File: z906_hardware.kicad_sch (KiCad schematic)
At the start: 23 parts, among them J1 USB_C_Receptacle_USB2.0_14P, J3 DE_15 Amplifier, J4 DE15 Console, U1 ESP32-S3-WROOM-1, U2 AP63203WU, U3 PCM5102A, U4 TPD2EUSB30, U5 TPD1E05U06DYA, U6 TPS7A4533, U7 PCM1860DBT

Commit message: esp32 power
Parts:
- added C10: 10uF, symbol Device:C
- added C11: 1uF, symbol Device:C
- added C9: 0.1uF, symbol Device:C
- added R4: 0, symbol Device:R
- added R5: 10K, symbol Device:R
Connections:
- net +3.3V: now also C10.1, C9.1, R4.1
- net GND: now also C10.2, C11.2, C9.2
- net +3.3V_esp: now reaches U1.2 (3V3)
- net +3.3V_esp: now also R4.2, R5.1
- net at U1.3 (EN): now also C11.1, R5.2
- net GPIO19 renamed USB_DN
- net GPIO20 renamed USB_DP
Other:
- moved on the sheet: U1

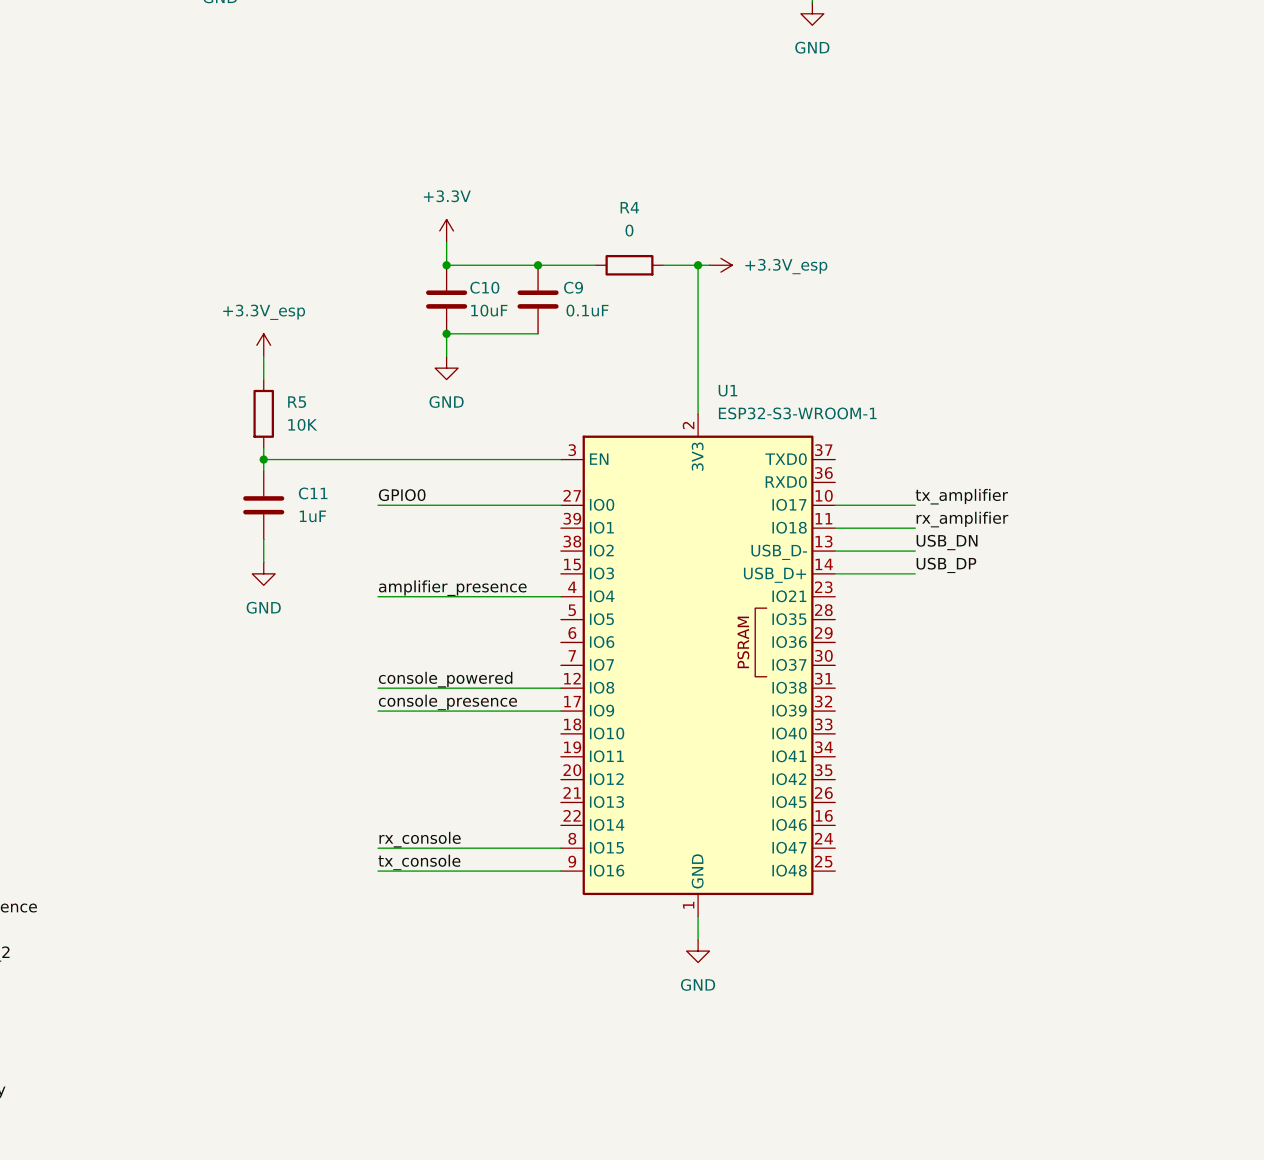
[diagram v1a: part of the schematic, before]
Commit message: jumper boot and reset
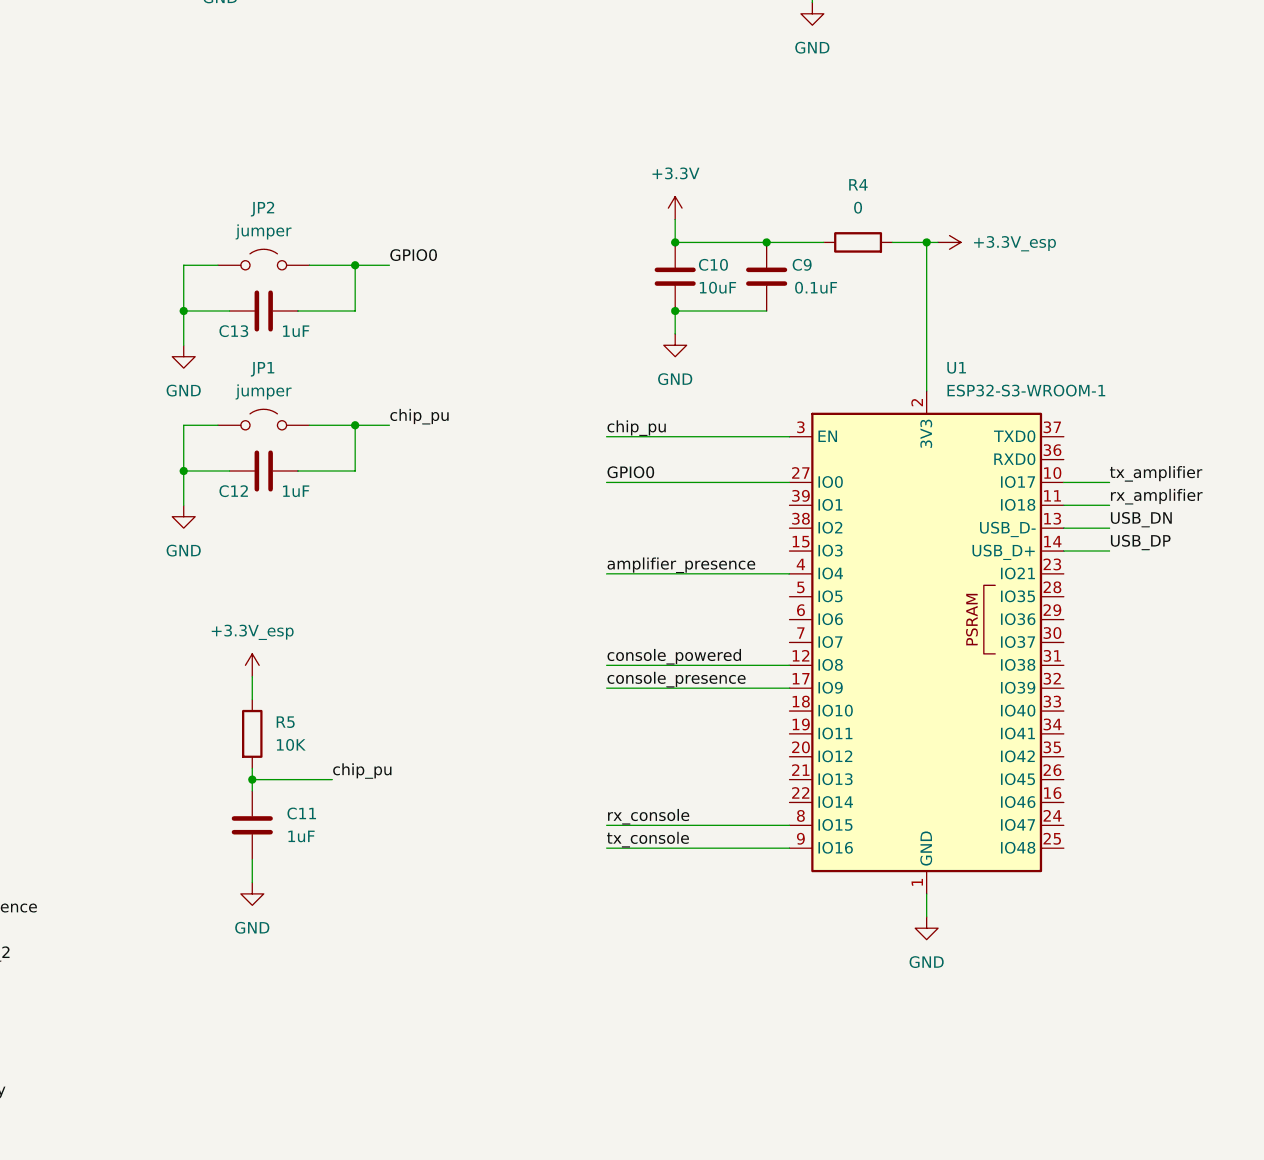
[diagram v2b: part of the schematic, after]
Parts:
- added C12, C13: 1uF, symbol Device:C
- added JP1, JP2: jumper, TestPoint:TestPoint_2Pads_Pitch2.54mm_Drill0.8mm, symbol Jumper:Jumper_2_Open
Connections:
- net GND: now also C12.1, C13.1, JP1.1 (A), JP2.1 (A)
- net GPIO0: now also C13.2, JP2.2 (B)
- net chip_pu: now reaches C11.1, R5.2, U1.3 (EN)
- net chip_pu: now also C12.2, JP1.2 (B)
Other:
- moved on the sheet: C10, C11, C9, R4, R5, U1

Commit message: PCM5102A
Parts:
- added C14, C16, C18, C21: 10uF, symbol Device:C
- added C15, C17, C19, C20: 0.1uF, symbol Device:C
- added C22, C23: 2.2uF, symbol Device:C
- added C24, C25: 2200pF, symbol Device:C
- added R6, R7: 470, symbol Device:R
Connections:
- net +3.3V: now also U3.17 (XSMT), U3.20 (DVDD), C16.1, C17.1
- net +3.3VA: now also U3.1 (CPVDD), U3.8 (AVDD), C14.1, C15.1, C18.1, C19.1
- net GND: now also U3.10 (DEMP), U3.11 (FLT), U3.12 (SCK), U3.16 (FMT), U3.19 (DGND), U3.3 (CPGND), U3.9 (AGND), C14.2, C15.2, C16.2, C17.2, C18.2, C19.2, C20.2, C21.2, C23.2, C24.2, C25.2
- net aux_left: now also C24.1, R6.2
- net aux_right: now also C25.1, R7.2
- net LCK: now reaches U1.5 (IO5)
- net LCK: now also U3.15 (LRCK)
- net BCK: now reaches U1.6 (IO6)
- net BCK: now also U3.13 (BCK)
- net DIN: now reaches U1.7 (IO7)
- net DIN: now also U3.14 (DIN)
- net at U3.18 (LDOO): now also C20.1, C21.1
- net at U3.2 (CAPP): now also C22.1
- net at U3.4 (CAPM): now also C22.2
- net at U3.5 (VNEG): now also C23.1
- net at U3.6 (OUTL): now also R6.1
- net at U3.7 (OUTR): now also R7.1
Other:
- moved on the sheet: C10, C11, C12, C13, C2, C3, C4, C5, C6, C7, C8, C9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

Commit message: PCM1860DBT
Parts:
- added C26, C28, C30, C32: 10uF, symbol Device:C
- added C27, C29, C31, C33: 0.1uF, symbol Device:C
- added C34: 1uF, symbol Device:C
- added C35, C37: 4.7uF, symbol Device:C
- added C36, C38: 1nF, symbol Device:C
- added J2: AudioJack3, symbol Connector_Audio:AudioJack3
- added R10, R11: 100k, symbol Device:R
- added R12, R9: 100, symbol Device:R
- added R8: 10K, symbol Device:R
- added U8: TPD2E2U06DCK, Package_TO_SOT_SMD:SOT-323_SC-70, symbol Power_Protection:TPD2E2U06DCK
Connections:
- net +3.3V: now also U7.13 (DVDD), U7.14 (IOVDD), C26.1, C27.1, C28.1, C29.1, R8.1
- net +3.3VA: now also U7.8 (AVDD), C30.1, C31.1
- net BCK: now also U7.17 (BCK)
- net GND: now also U7.10 (XI), U7.12 (DGND), U7.20 (MD6), U7.21 (MD5), U7.22 (MD4), U7.23 (MD2), U7.24 (MD3), U7.25 (MD1), U7.26 (MD0), U7.7 (AGND), C26.2, C27.2, C28.2, C29.2, C30.2, C31.2, C32.2, C33.2, C34.2, C36.1, C38.1, J2.S, R10.1, R11.1, U8.3; no longer U3.12 (SCK)
- net LCK: now also U7.16 (LRCK)
- net at U7.11 (LDO): now also C32.1, C33.1
- net MCLK: now reaches U7.15 (SCKI)
- net MCLK: now also U1.19 (IO11), U3.12 (SCK)
- net ADC_DATA: now reaches U7.18 (DOUT)
- net ADC_DATA: now also U1.7 (IO7)
- net at U7.19 (INT): now also R8.2
- net at U7.3 (VINL1/VIN1P): now also C36.2, R9.2
- net at U7.4 (VINR1/VIN2P): now also C38.2, R12.2
- net at U7.6 (VREF): now also C34.1
- net DAC_DATA: now reaches U1.18 (IO10)
- net DAC_DATA: now also U3.14 (DIN)
- removed net DIN: U1.7 (IO7), U3.14 (DIN)
- new net: C35.1, J2.T, R10.2, U8.1
- new net: C37.1, J2.R, R11.2, U8.2
- new net: C37.2, R12.1
- new net: C35.2, R9.1
- no-connect marks 2 -> 9
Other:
- moved on the sheet: C10, C11, C12, C13, C14, C15, C16, C17, C18, C19, C20, C21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

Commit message: various correction
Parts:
- removed FB1: 600 Ohm @ 100 Mhz, 500ma, symbol Device:FerriteBead
- removed R3: 4.7, symbol Device:R
- removed R8: 10K, symbol Device:R
- C10: value 10uF -> 22uF
- C12, C13: value 1uF -> 0.1uF
- C24, C25: value 2200pF -> 2.2nF
- C34: value 1uF -> 2.2uF
- C5: value 20uF -> 22uF
- C6: value 22uF -> 10uF
- U6: footprint Package_TO_SOT_SMD:TO-263-5_TabPin3 -> Package_TO_SOT_SMD:SOT-223-6_TabPin3
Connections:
- net +5V: now also C6.1, U6.1 (~{SHDN}), U6.2 (IN)
- no-connect marks 9 -> 10

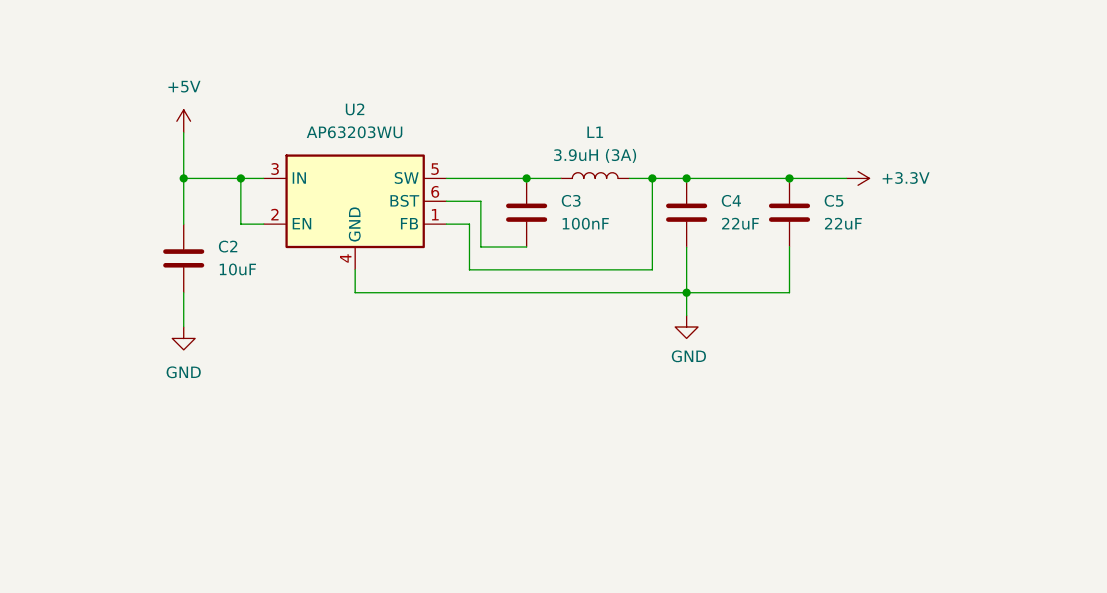
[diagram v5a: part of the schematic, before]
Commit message: change 3.3v regulator
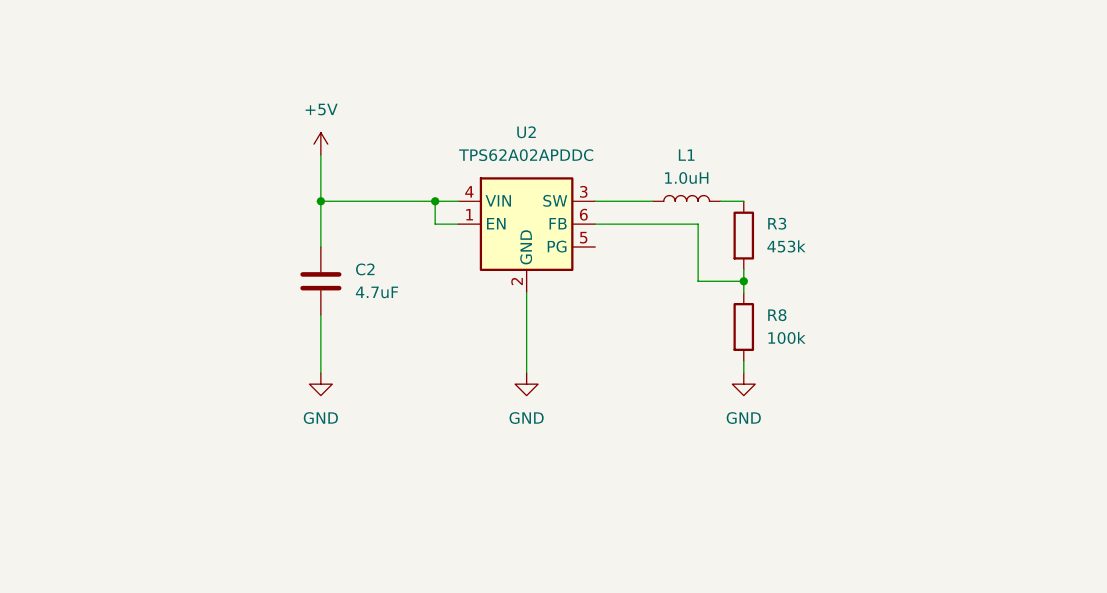
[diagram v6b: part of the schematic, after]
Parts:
- removed C3: 100nF, symbol Device:C
- removed C4, C5: 22uF, symbol Device:C
- removed U2: AP63203WU, Package_TO_SOT_SMD:TSOT-23-6, symbol Regulator_Switching:AP63203WU
- added R3: 453k, symbol Device:R
- added R8: 100k, symbol Device:R
- added U2: TPS62A02APDDC, Package_TO_SOT_SMD:SOT-23-6, symbol Regulator_Switching:TPS62A02APDDC
- C2: value 10uF -> 4.7uF
- L1: value 3.9uH (3A) -> 1.0uH
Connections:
- net +3.3V: no longer L1.2
- net +5V: now also U2.1 (EN), U2.4 (VIN)
- net GND: now also R8.2, U2.2 (GND)
- net at L1.1: now also U2.3 (SW)
- new net: R3.2, R8.1, U2.6 (FB)
- new net: L1.2, R3.1

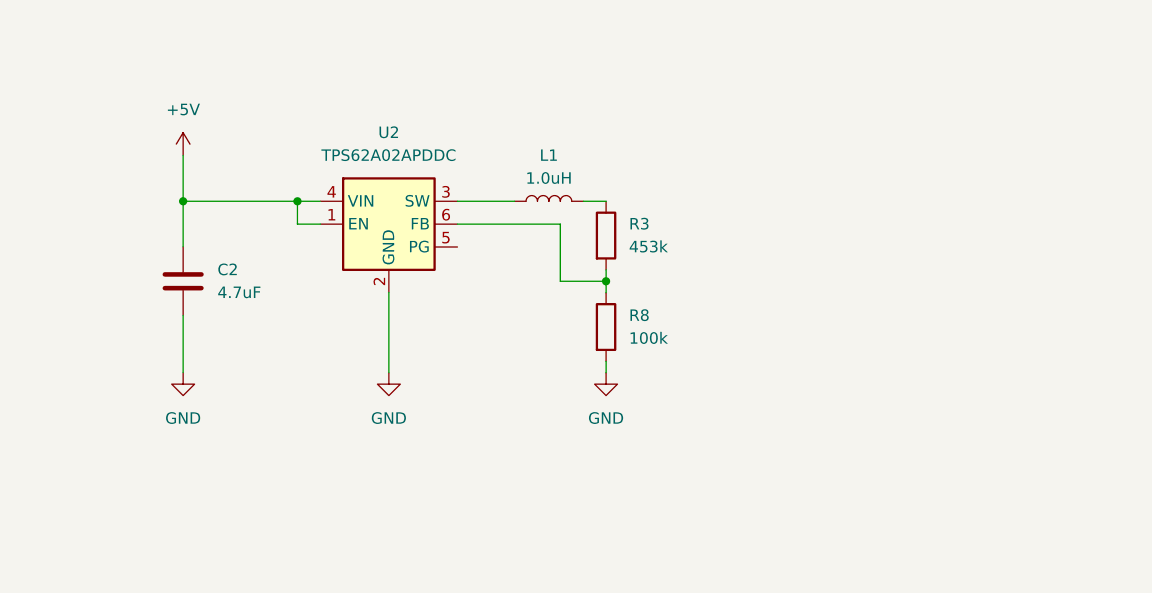
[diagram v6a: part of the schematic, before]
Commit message: TPS62A02APDDC 3.3 power
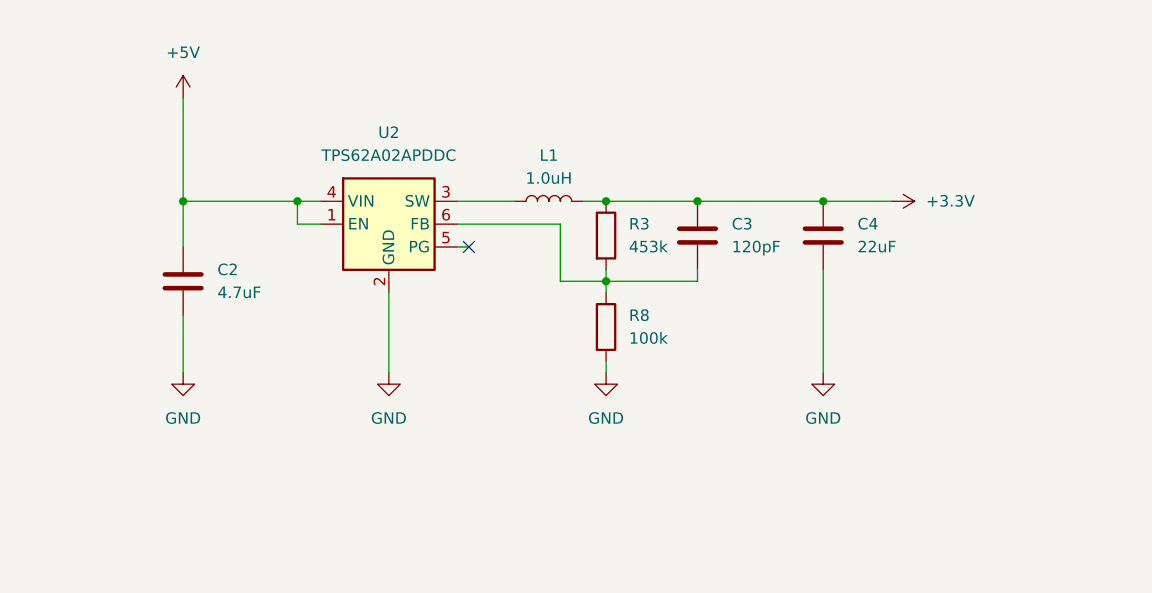
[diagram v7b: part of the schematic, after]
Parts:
- added C3: 120pF, symbol Device:C
- added C4: 22uF, symbol Device:C
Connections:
- net +3.3V: now also L1.2, R3.1, C3.1, C4.1
- net GND: now also C4.2
- net at R3.2, R8.1, U2.6 (FB): now also C3.2
- no-connect marks 10 -> 11
